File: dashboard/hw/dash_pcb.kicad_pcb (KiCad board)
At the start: 2 copper layers, 180 x 65 mm, 35 parts, among them J1 LCD, J2 DEBUG, J3 LCD_BL, J4 CAR, U1 LPC11C24FBD48, U2 TPS62175, U3 TLV70233_SOT23-5, Y1 12MHz

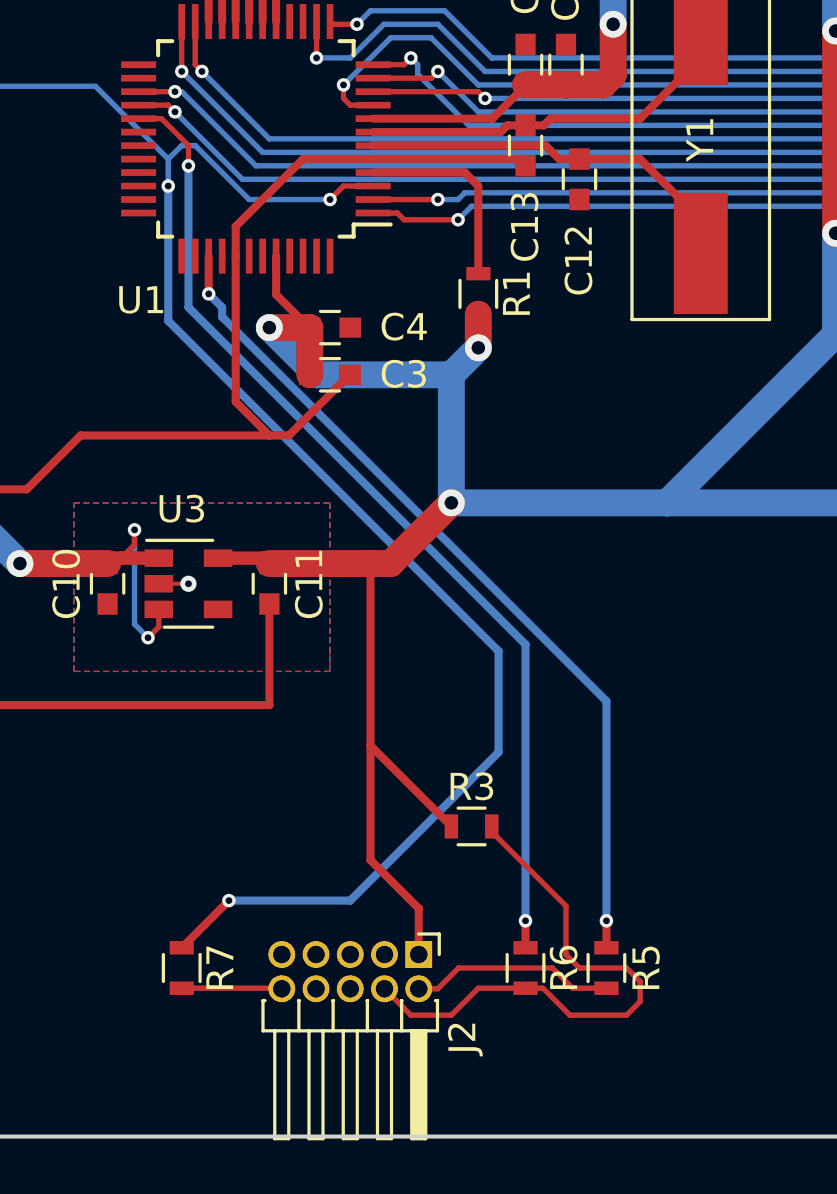
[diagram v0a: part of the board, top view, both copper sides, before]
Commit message: make shrouded version of programming connector
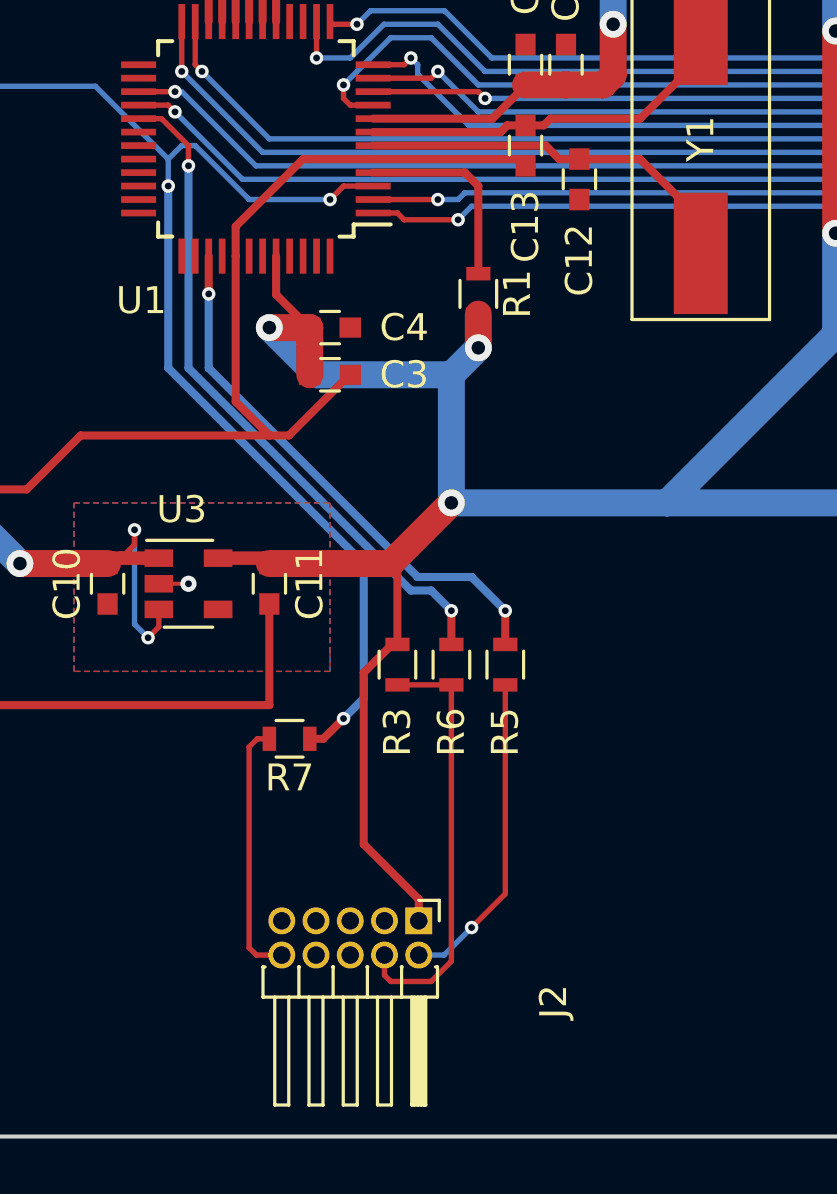
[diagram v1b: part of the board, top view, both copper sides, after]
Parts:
- J2: footprint Pin_Headers:Pin_Header_Angled_2x05_Pitch1.27mm -> custom_footprints:Pin_Header_Angled_2x05_Pitch1.27mm_AMPHENOL_SHROUDED
- moved R5 11.9 mm to (236.8, 102.5)
- moved R6 11.6 mm to (234.8, 102.5)
- moved R7 9.39 mm to (228.8, 105.2), turned to 180 degrees
- moved R3 6.60 mm to (232.8, 102.5), turned to 270 degrees
- moved J2 1.25 mm to (233.5, 112.0)
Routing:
- net /5VPG: track 67.7 -> 51.5 mm
- net /SWCLK: track 37.2 -> 25.2 mm
- net /SWDIO: track 31.8 -> 20.1 mm
- net Net-(J2-Pad10): track 3.72 -> 9.65 mm
- net Net-(J2-Pad4): track 20.7 -> 15.9 mm
- net +3V3: track 165.7 -> 161.1 mm
- net Net-(J2-Pad2): track 7.59 -> 11.9 mm, vias 0 -> 1

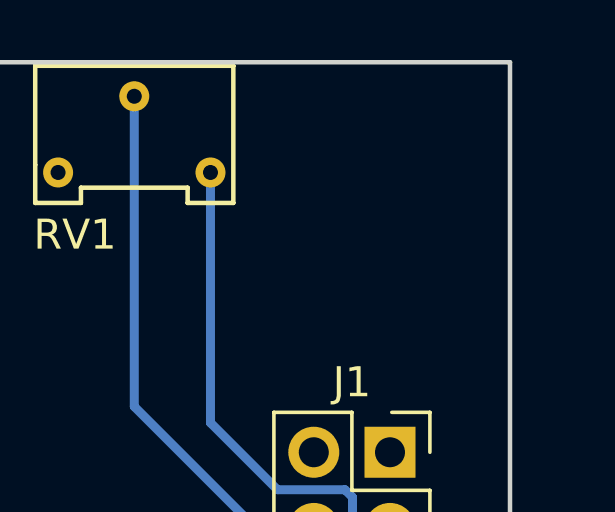
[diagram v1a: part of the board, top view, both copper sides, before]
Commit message: add test mounting hole
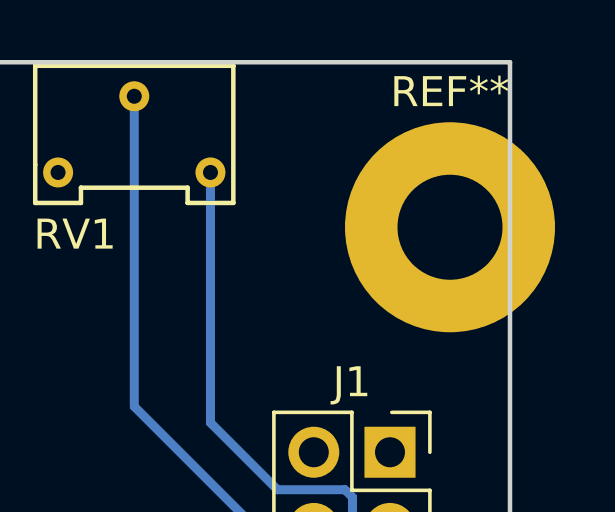
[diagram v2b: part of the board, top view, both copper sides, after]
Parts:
- added REF**: SolderWirePad_single_2-5mmDrill, Mounting_Holes:MountingHole_3.5mm_Pad, F.Cu at (263.0, 60.5)
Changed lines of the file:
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@@
     (links 111)
     (no_connects 0)
-    (area 84.924999 54.924999 265.075001 120.075001)
+    (area 84.924999 52.923 275.959525 120.225001)
     (thickness 1.6)
-    (drawings 4)
+    (drawings 5)
     (tracks 374)
     (zones 0)
-    (modules 35)
+    (modules 36)
     (nets 59)
   )
@@
   )
   (setup
-    (last_trace_width 0.3)
+    (last_trace_width 0.15)
     (user_trace_width 0.2)
     (user_trace_width 0.3)
@@
     )
   )
+  (module Mounting_Holes:MountingHole_3.5mm_Pad (layer F.Cu)
+    (at 263 60.5)
+    (descr "Mounting Hole 3.5mm")
+    (tags "mounting hole 3.5mm")
+    (attr virtual)
+    (fp_text reference REF** (at 0 -4.5) (layer F.SilkS)
+      (effects (font (size 1 1) (thickness 0.15)))
+    )
+    (fp_text value SolderWirePad_single_2-5mmDrill (at 0 4.5) (layer F.Fab)
+      (effects (font (size 1 1) (thickness 0.15)))
+    )
+    (fp_text user %R (at 0.3 0) (layer F.Fab)
+      (effects (font (size 1 1) (thickness 0.15)))
+    )
+    (fp_circle (center 0 0) (end 3.5 0) (layer Cmts.User) (width 0.15))
+    (fp_circle (center 0 0) (end 3.75 0) (layer F.CrtYd) (width 0.05))
+    (pad 1 thru_hole circle (at 0 0) (size 7 7) (drill 3.5) (layers *.Cu *.Mask))
+  )
+  (gr_arc (start 263 60.5) (end 263 62.3) (angle 183.0127591) (layer F.CrtYd) (width 0.2))
   (gr_line (start 265 120) (end 265 55) (layer Edge.Cuts) (width 0.15))
   (gr_line (start 85 120) (end 265 120) (layer Edge.Cuts) (width 0.15))

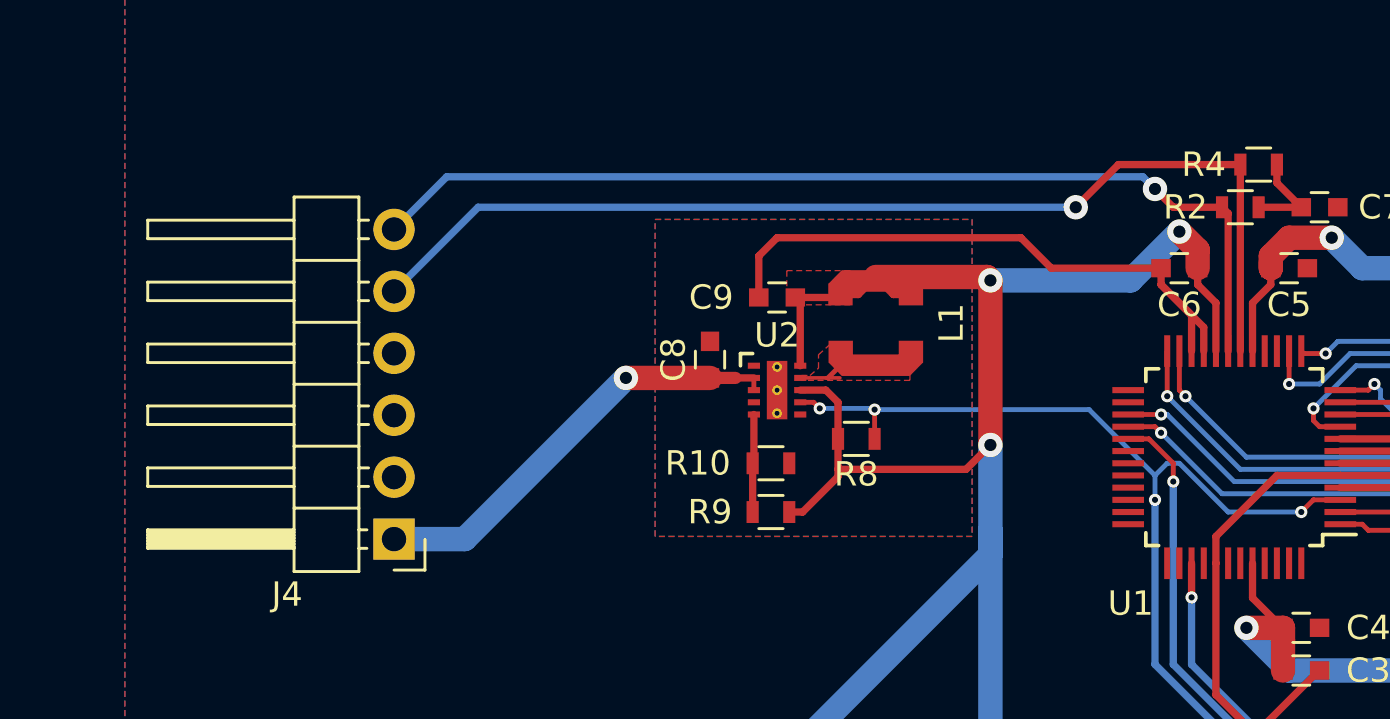
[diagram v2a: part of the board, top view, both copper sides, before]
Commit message: use 4 position connector for car interface
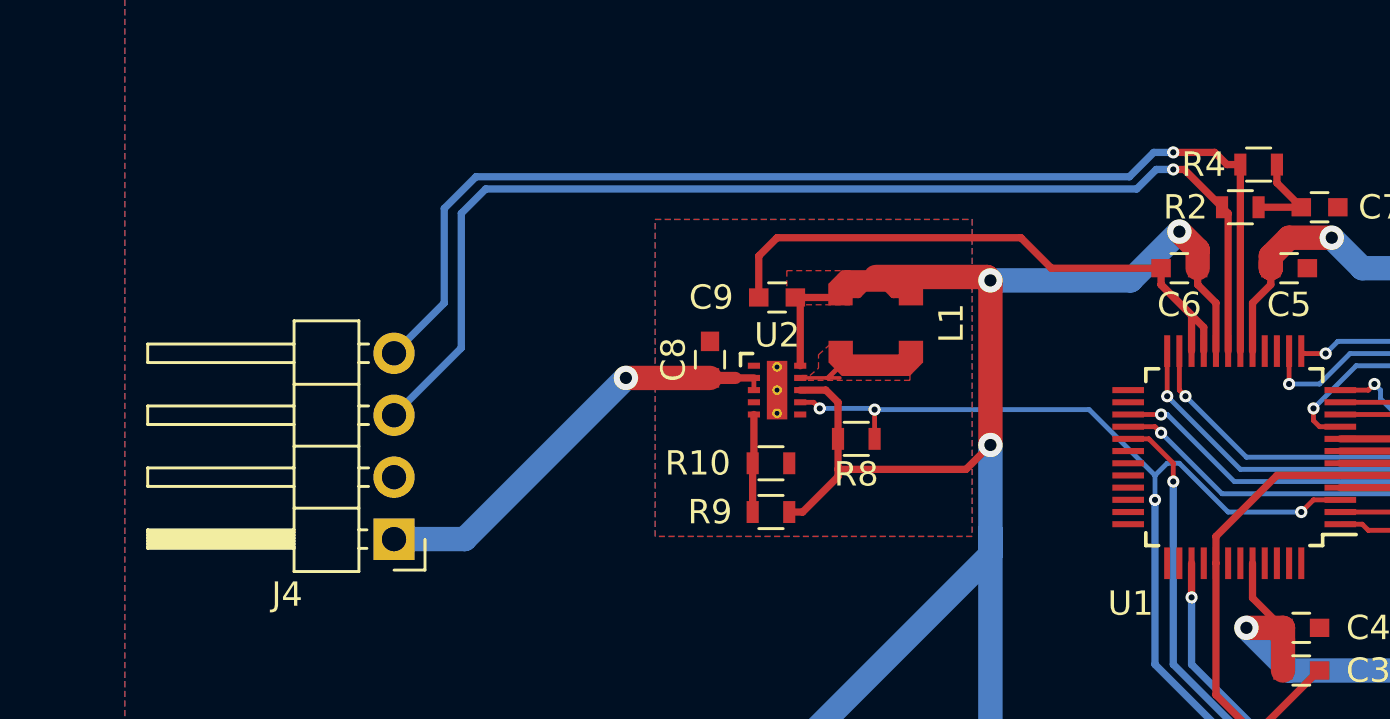
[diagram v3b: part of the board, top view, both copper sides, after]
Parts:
- J4: footprint Pin_Headers:Pin_Header_Angled_1x06_Pitch2.54mm -> Pin_Headers:Pin_Header_Angled_1x04_Pitch2.54mm
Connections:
- J4 pad 3: GND -> /CANH
- J4 pad 4: GND -> /CANL
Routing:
- net /CANH: track 41.4 -> 48.0 mm
- net /CANL: track 44.5 -> 48.3 mm

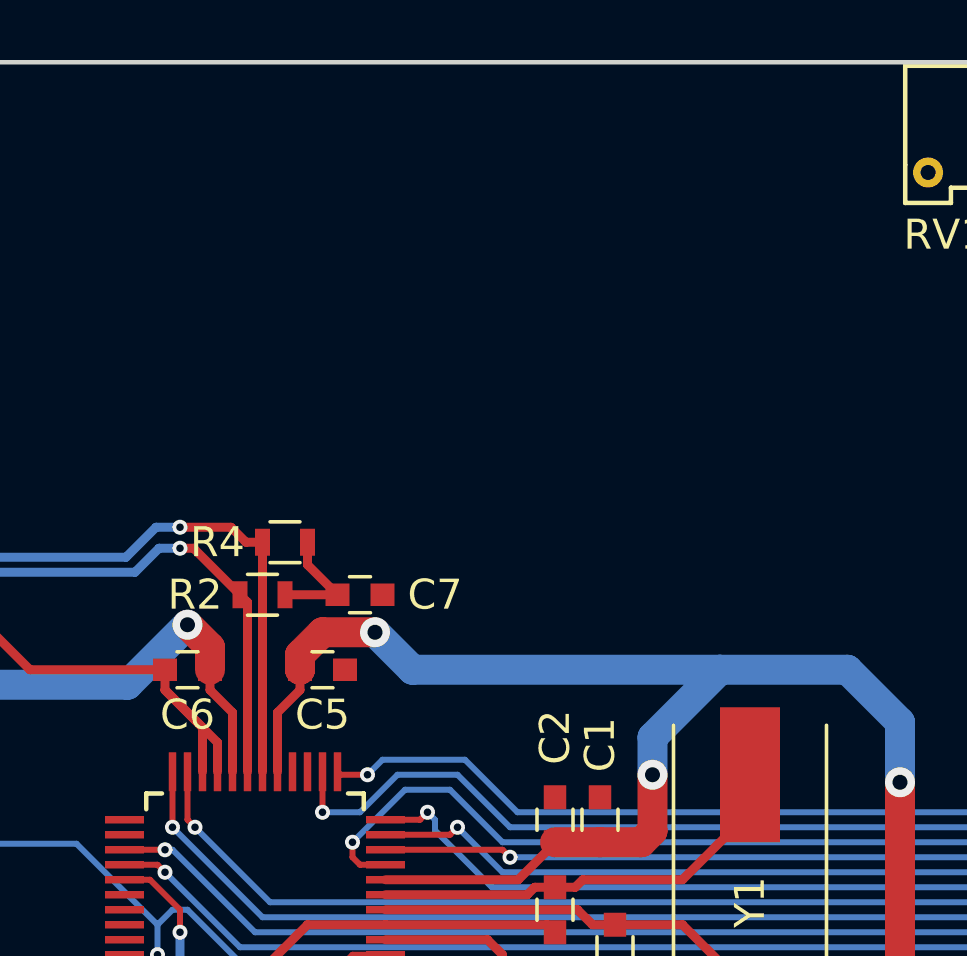
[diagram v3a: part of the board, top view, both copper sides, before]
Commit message: add jumpers to selectively terminate can bus
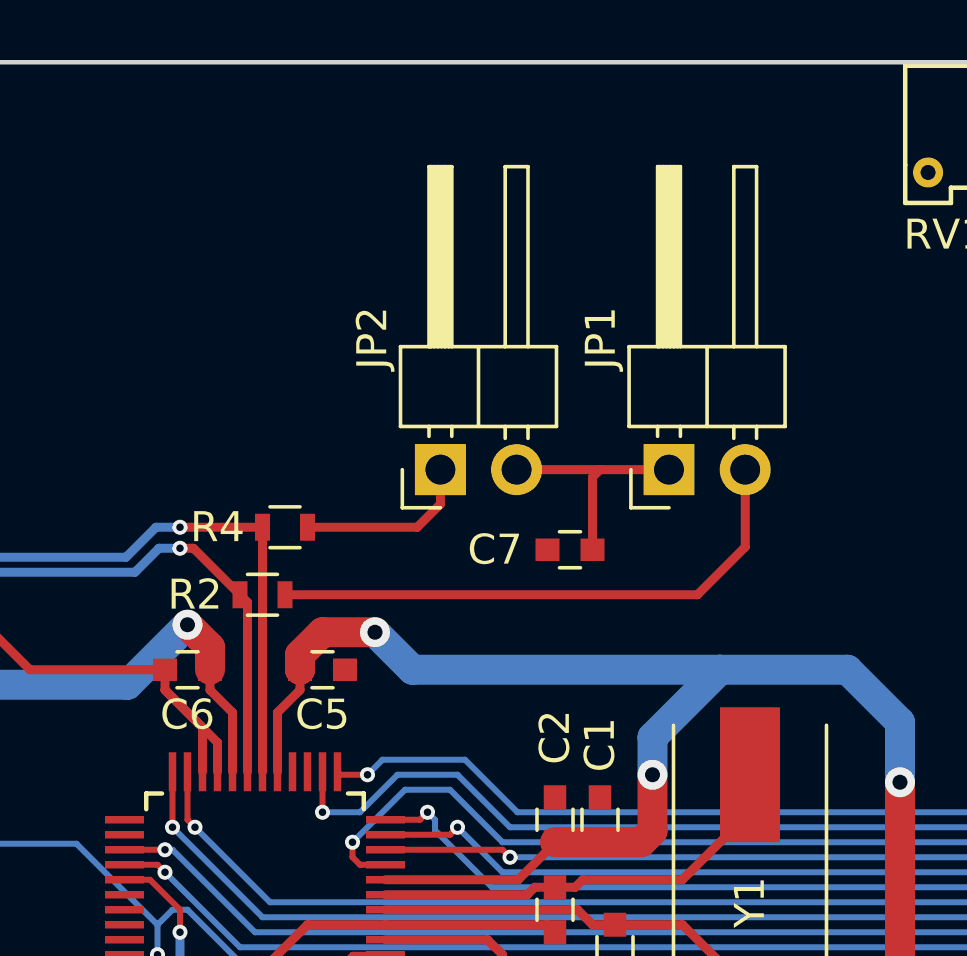
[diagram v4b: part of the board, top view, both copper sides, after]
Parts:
- added JP1: TERMH, Pin_Headers:Pin_Header_Angled_1x02_Pitch2.54mm, F.Cu at (241.3, 68.6)
- added JP2: TERML, Pin_Headers:Pin_Header_Angled_1x02_Pitch2.54mm, F.Cu at (233.7, 68.6)
- moved C7 7.16 mm to (238.0, 71.2), turned to 180 degrees
- moved R4 0.50 mm to (228.5, 70.5)
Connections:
- R2 pad 1: Net-(C7-Pad1) -> Net-(JP1-Pad2)
- R4 pad 1: Net-(C7-Pad1) -> Net-(JP2-Pad1)
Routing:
- net Net-(JP1-Pad2): track 0.00 -> 18.6 mm
- net Net-(JP2-Pad1): track 0.00 -> 5.90 mm
- net Net-(C7-Pad1): track 3.91 -> 7.85 mm

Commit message: pull reset to 3.3 instead of 5
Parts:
- moved R8 31.5 mm to (230.8, 107.5)
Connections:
- R7 pad 1: /5VPG -> /MCU_~RESET
- R8 pad 1: /5VPG -> +3V3
- R8 pad 2: +5V -> /MCU_~RESET
- U1 pad 3: /5VPG -> /MCU_~RESET
- U2 pad 7: /5VPG -> /MCU_~RESET
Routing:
- net /MCU_~RESET: track 0.00 -> 53.0 mm, vias 0 -> 3
- net /5VPG: track 51.5 -> 0.00 mm, vias 5 -> 0

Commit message: change termination jumpers to dip switches
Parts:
- removed JP1: TERMH, Pin_Headers:Pin_Header_Angled_1x02_Pitch2.54mm
- removed JP2: TERML, Pin_Headers:Pin_Header_Angled_1x02_Pitch2.54mm
- removed REF**: SolderWirePad_single_2-5mmDrill, Mounting_Holes:MountingHole_3.5mm_Pad
- added SW1: CONFIG, Buttons_Switches_THT:SW_DIP_x4_W7.62mm_Slide, F.Cu at (233.7, 68.6)
- moved C7 10.8 mm to (229.2, 65.0), turned to 270 degrees
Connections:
- R2 pad 1: Net-(JP1-Pad2) -> /CANH_TERM
- R4 pad 1: Net-(JP2-Pad1) -> /CANL_TERM
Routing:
- net Net-(JP1-Pad2): track 18.6 -> 0.00 mm
- net /CANH_TERM: track 0.00 -> 10.7 mm
- net Net-(JP2-Pad1): track 5.90 -> 0.00 mm
- net /CANL_TERM: track 0.00 -> 5.90 mm

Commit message: add mounting holes to match lcd
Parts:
- added REF**: LCD_mount, custom_footprints:LCD_mount, F.Cu at (265.0, 114.5)
- added REF**: LCD_mount, custom_footprints:LCD_mount, F.Cu at (265.0, 60.5)
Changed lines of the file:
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@@
     (area 84.924999 54.924999 265.075001 120.075001)
     (thickness 1.6)
-    (drawings 5)
+    (drawings 4)
     (tracks 388)
     (zones 0)
-    (modules 36)
+    (modules 38)
     (nets 65)
   )
@@
   )
   (setup
-    (last_trace_width 0.3)
+    (last_trace_width 0.15)
     (user_trace_width 0.2)
     (user_trace_width 0.3)
@@
     (add_net "Net-(U1-Pad48)")
   )
+  (module custom_footprints:LCD_mount locked (layer F.Cu)
+    (at 265 114.5)
+    (fp_text reference REF** (at 0 4.5) (layer F.SilkS) hide
+      (effects (font (size 1 1) (thickness 0.15)))
+    )
+    (fp_text value LCD_mount (at 0 -4.5) (layer F.Fab)
+      (effects (font (size 1 1) (thickness 0.15)))
+    )
+    (pad 1 thru_hole oval (at 0 0) (size 12 7.5) (drill oval 8 3.5) (layers *.Cu *.Mask))
+  )
   (module Housings_QFP:LQFP-48_7x7mm_Pitch0.5mm (layer F.Cu)
     (at 227.5 83 180)
@@
     )
   )
-  (gr_arc (start 263 60.5) (end 263 62.3) (angle 183.0127591) (layer F.CrtYd) (width 0.2))
+  (module custom_footprints:LCD_mount locked (layer F.Cu)
+    (at 265 60.5)
+    (fp_text reference REF** (at 0 4.5) (layer F.SilkS) hide
+      (effects (font (size 1 1) (thickness 0.15)))
+    )
+    (fp_text value LCD_mount (at 0 -4.5) (layer F.Fab)
+      (effects (font (size 1 1) (thickness 0.15)))
+    )
+    (pad 1 thru_hole oval (at 0 0) (size 12 7.5) (drill oval 8 3.5) (layers *.Cu *.Mask))
+  )
   (gr_line (start 265 120) (end 265 55) (layer Edge.Cuts) (width 0.15))
   (gr_line (start 85 120) (end 265 120) (layer Edge.Cuts) (width 0.15))

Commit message: crunch board a bunch
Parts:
- moved J2 26.7 mm to (256.9, 99.1), turned to 0 degrees
- moved R7 23.5 mm to (252.2, 106.0), turned to 0 degrees
- moved R8 21.8 mm to (252.2, 103.8), turned to 0 degrees
- moved R3 19.5 mm to (252.2, 101.2), turned to 0 degrees
- moved R6 17.8 mm to (252.2, 99.2), turned to 0 degrees
- moved R5 16.3 mm to (252.2, 97.2), turned to 180 degrees
- moved C7 7.94 mm to (233.0, 58.0)
- moved C1 7.00 mm to (246.0, 80.2)
- moved C10 7.00 mm to (229.0, 99.5)
- moved C11 7.00 mm to (235.0, 99.5)
- moved C12 7.00 mm to (246.5, 84.5)
- moved C13 7.00 mm to (244.5, 83.2)
- moved C2 7.00 mm to (244.5, 80.2)
- moved C3 7.00 mm to (237.2, 91.8)
- moved C4 7.00 mm to (237.2, 90.0)
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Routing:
- net /MCU_~RESET: track 53.0 -> 64.1 mm
- net +3V3: track 161.1 -> 152.8 mm
- net /SWCLK: track 25.2 -> 33.2 mm
- net /LCD_DB7: track 38.0 -> 31.0 mm
- net /LCD_DB5: track 37.7 -> 30.7 mm
- net /LCD_DB2: track 30.4 -> 23.4 mm
- net /LCD_~WR: track 43.7 -> 36.7 mm
- net /LCD_~RD: track 40.1 -> 33.1 mm
- net /LCD_DB6: track 40.8 -> 33.8 mm
- net /LCD_DB4: track 39.6 -> 32.6 mm
- net /LCD_DB3: track 28.3 -> 21.3 mm
- net /LCD_DB1: track 34.9 -> 27.9 mm
- net /LCD_DB0: track 30.6 -> 23.6 mm
- net /LCD_~RST: track 32.0 -> 25.0 mm
- net /LCD_C/~D: track 31.5 -> 24.5 mm
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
